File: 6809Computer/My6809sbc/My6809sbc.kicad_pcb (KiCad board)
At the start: 2 copper layers, 155 x 114 mm, 62 parts, among them J1 HEADER 2x5, J10 TP3, J11 A.OUT, J12 HEADER 2x20, J13 5V IN, J2 HEADER 1x6, J3 HEADER 2x5, J4 HEADER 2x5, J5 TP1, J6 TP2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

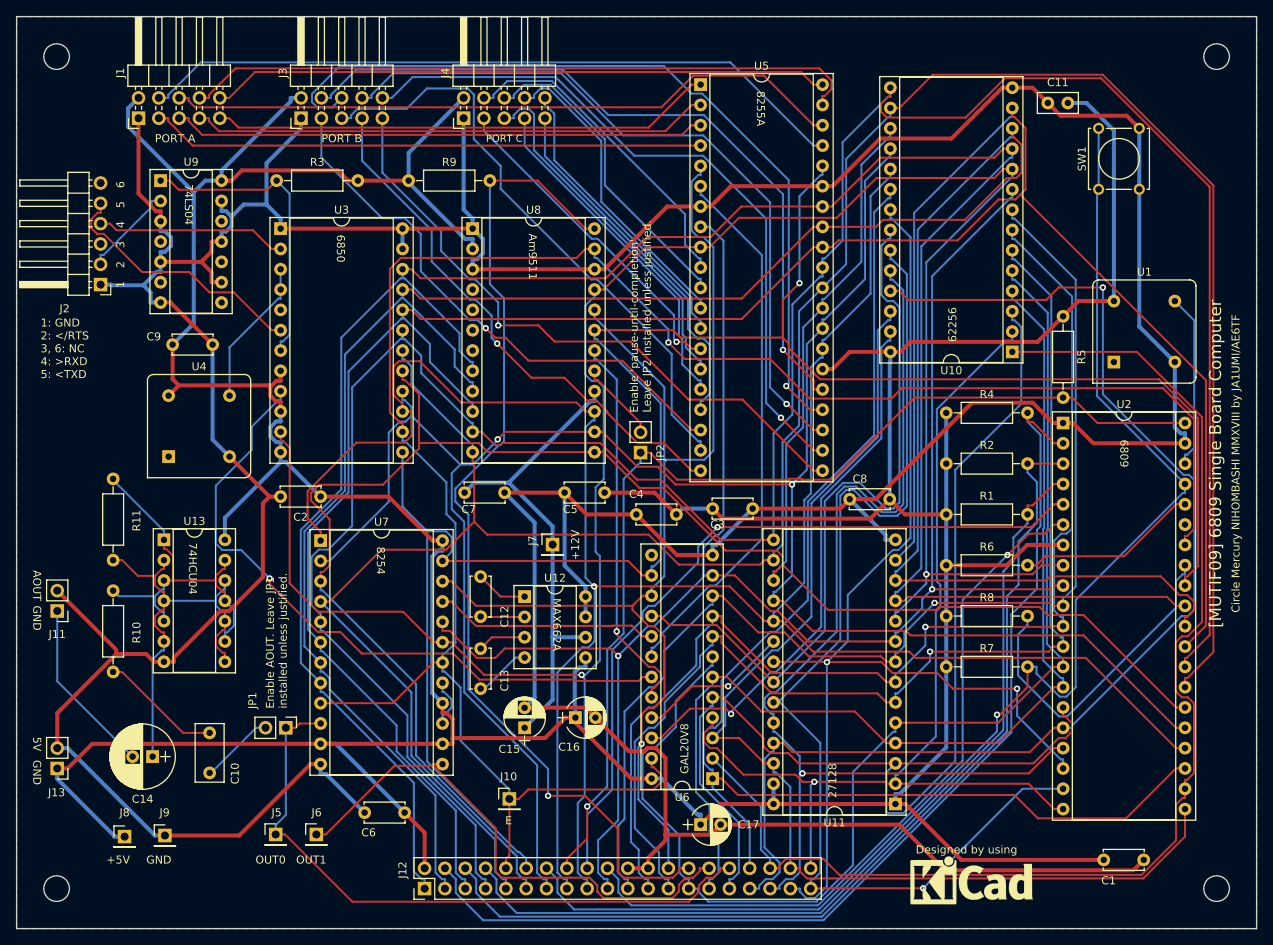
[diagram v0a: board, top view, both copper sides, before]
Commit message: Update design files of 6809 SBC
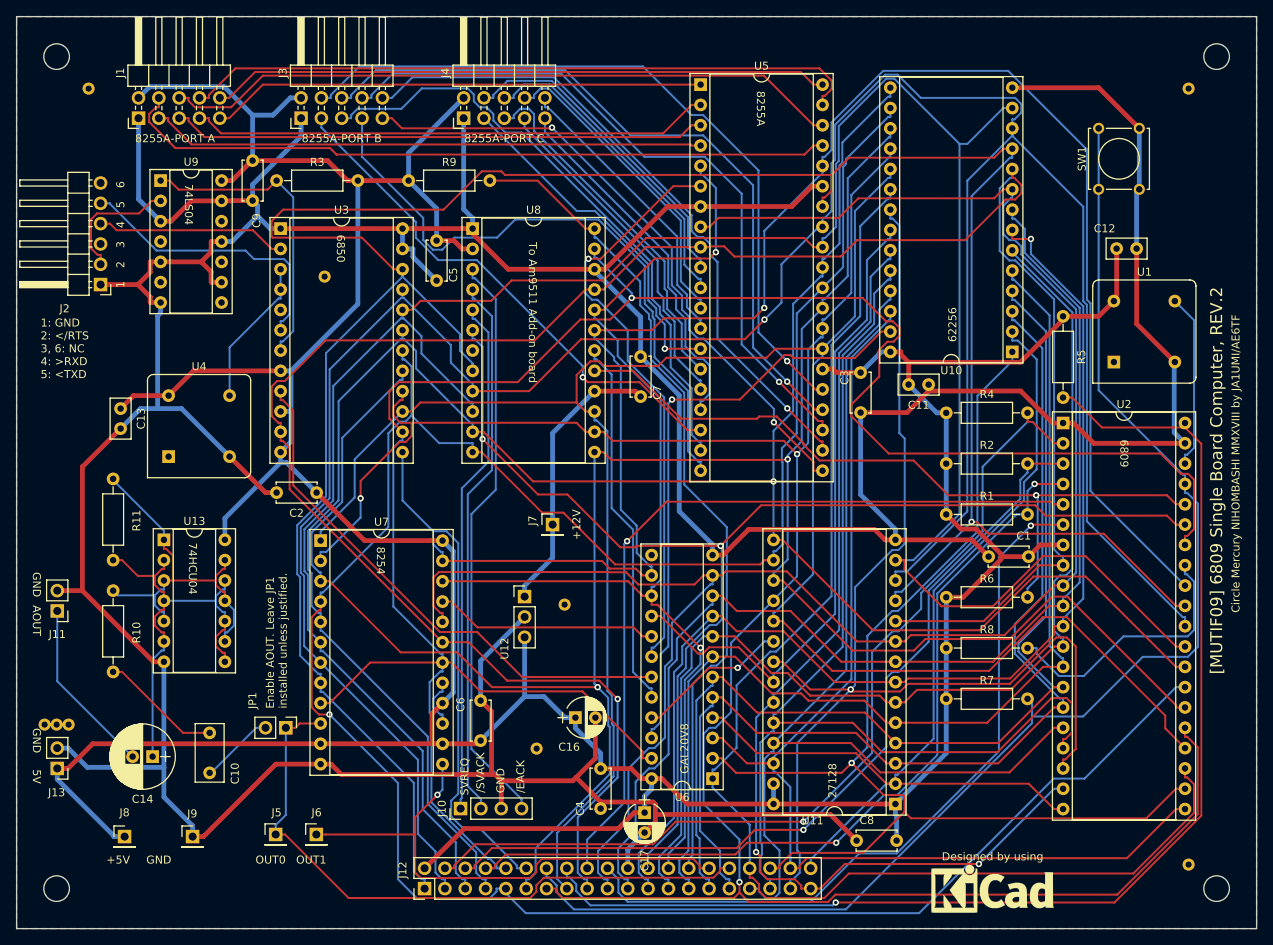
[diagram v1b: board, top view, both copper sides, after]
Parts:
- removed C15: 4.7u, Capacitors_THT:CP_Radial_D5.0mm_P2.50mm
- removed JP2: Enable 'Pause-until-completion', Pin_Headers:Pin_Header_Straight_1x02_Pitch2.54mm
- added REF**: via, mylib:via, F.Cu at (88.5, 62.5)
- added REF**: via, mylib:via, F.Cu at (118.5, 103.5)
- added REF**: via, mylib:via, F.Cu at (115.0, 121.5)
- added REF**: via, mylib:via, F.Cu at (59.0, 39.0)
- added REF**: via, mylib:via, F.Cu at (196.5, 39.0)
- added REF**: via, mylib:via, F.Cu at (196.5, 136.0)
- added REF**: via, mylib:via, F.Cu at (56.5, 118.5)
- added REF**: via, mylib:via, F.Cu at (55.0, 118.5)
- added REF**: via, mylib:via, F.Cu at (53.5, 118.5)
- C12, C13: value 0.22u -> 0.1u; footprint Capacitors_THT:C_Disc_D5.0mm_W2.5mm_P5.00mm -> Capacitors_THT:C_Disc_D5.0mm_W2.5mm_P2.50mm
- C16: value 4.7u -> 47u
- J10: value TP3 -> Conn_01x04; footprint Pin_Headers:Pin_Header_Straight_1x01_Pitch2.54mm -> Pin_Headers:Pin_Header_Straight_1x04_Pitch2.54mm
- J11: value A.OUT -> AUDIO OUT
- J13: value 5V IN -> Conn_01x02
- JP1: value A.OUT enable (normally inst'd) -> PIT Test (normally installed)
- U12: value MAX662A -> U3V12F12; footprint Housings_DIP:DIP-8_W7.62mm_Socket -> Pin_Headers:Pin_Header_Straight_1x03_Pitch2.54mm
- moved C12 91.8 mm to (187.5, 59.0), turned to 0 degrees
- moved C13 54.1 mm to (63.0, 79.0)
- moved C8 42.7 mm to (155.0, 133.0)
- moved C1 39.1 mm to (176.5, 97.5), turned to 180 degrees
- moved C11 38.2 mm to (164.0, 76.0), turned to 180 degrees
- moved C4 37.0 mm to (123.0, 129.0), turned to 90 degrees
- moved C5 31.0 mm to (102.5, 63.0), turned to 90 degrees
- moved C3 25.1 mm to (155.5, 74.5), turned to 270 degrees
- moved C9 25.1 mm to (79.5, 48.0), turned to 270 degrees
- moved C7 25.1 mm to (128.0, 77.5), turned to 90 degrees
- moved C6 13.1 mm to (108.0, 120.5), turned to 90 degrees
- moved C17 7.16 mm to (128.5, 129.5), turned to 270 degrees
- moved J10 6.21 mm to (105.5, 129.0), turned to 90 degrees
- moved R6 4.00 mm to (166.2, 102.6)
- moved R7 4.00 mm to (166.2, 115.3)
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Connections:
- C12 pad 1: Net-(C12-Pad1) -> /+5V
- C12 pad 2: Net-(C12-Pad2) -> /GND
- C13 pad 1: Net-(C13-Pad1) -> /+5V
- C13 pad 2: Net-(C13-Pad2) -> /GND
- J10 pad 1: /E -> Net-(J10-Pad1)
- J12 pad 24: /GND -> /Q
- R6 pad 2: Net-(R6-Pad2) -> /MRDY
- U12 pad 1: Net-(C12-Pad2) -> /+12V
- U12 pad 2: Net-(C12-Pad1) -> /GND
- U12 pad 3: Net-(C13-Pad1) -> /+5V
- U2 pad 35: Net-(U2-Pad35) -> /Q
- U2 pad 36: Net-(R6-Pad2) -> /MRDY
- U8 pad 17: Net-(JP2-Pad2) -> /MRDY
- U8 pad 3: /GND -> Net-(J10-Pad4)
- U8 pad 4: Net-(U8-Pad4) -> Net-(J10-Pad2)
- U8 pad 5: Net-(U8-Pad5) -> Net-(J10-Pad1)
- U8 pad 6: Net-(U8-Pad6) -> /Q
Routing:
- net /Q: track 0.00 -> 155.5 mm, vias 0 -> 2
- net /MRDY: track 0.00 -> 94.4 mm, vias 0 -> 1
- net /+5V: track 594.1 -> 513.0 mm
- net Net-(J10-Pad4): track 0.00 -> 72.6 mm
- net Net-(J10-Pad2): track 0.00 -> 67.9 mm
- net Net-(J10-Pad1): track 0.00 -> 64.8 mm
- net /D3: track 321.1 -> 266.8 mm, vias 0 -> 1
- net /D1: track 299.1 -> 337.2 mm, vias 0 -> 1
- net /D0: track 288.3 -> 320.9 mm, vias 0 -> 1
- net /A8: track 156.1 -> 127.5 mm, vias 1 -> 0
- net /A7: track 159.8 -> 132.0 mm
- net /GND: track 655.7 -> 628.9 mm
- net /+12V: track 60.7 -> 35.3 mm
- net //HALT: track 130.9 -> 153.8 mm
- net Net-(R6-Pad2): track 22.8 -> 0.00 mm
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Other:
- net class Power: trace_width 0.5 -> 0.6
- board text added: "/EACK"
- board text added: "/SVACK"
- board text added: "8255A-PORT A"
- board text added: "8255A-PORT B"
- board text added: "8255A-PORT C"
- board text added: "SVREQ"
- board text added: "To Am9511 Add-on board"
- board text added: "[MUTIF09] 6809 Single Board Computer, REV.2"
- board text removed: "Am9511"
- board text removed: "E"
- board text removed: "Enable 'pause-until-completion' Leave JP2 installed unless justified."
- board text removed: "MAX662A"
- board text removed: "PORT A"
- board text removed: "PORT B"
- board text removed: "PORT C"
- board text removed: "[MUTIF09] 6809 Single Board Computer"

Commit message: Update design materials of 6809sbc and old files are moved to the archive directory (REV2). Now My6809sbc directory contains REV3 design materials.
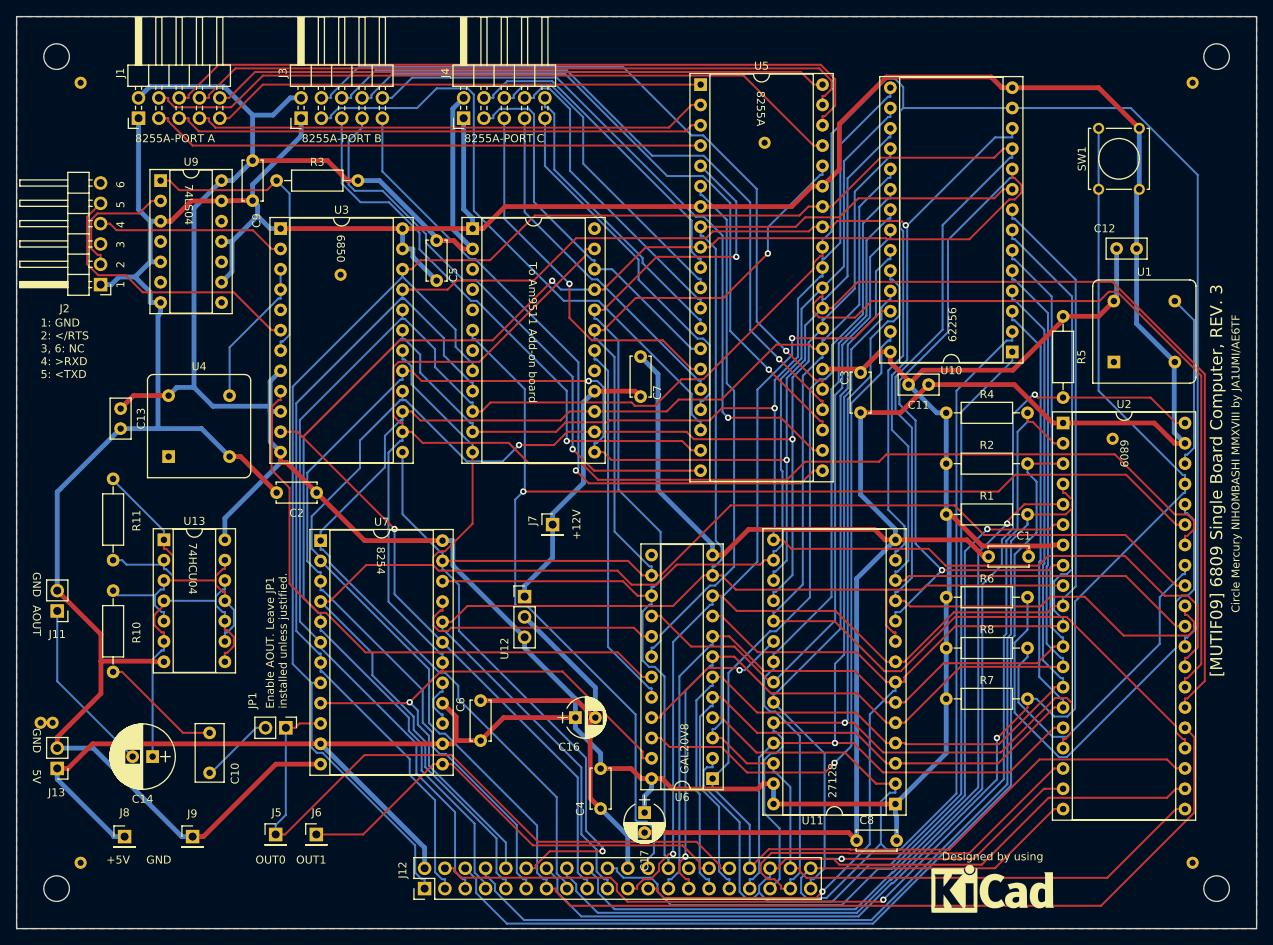
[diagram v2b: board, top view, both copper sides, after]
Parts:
- removed J10: Conn_01x04, Pin_Headers:Pin_Header_Straight_1x04_Pitch2.54mm
- removed R9: 2.2k, Resistors_THT:R_Axial_DIN0207_L6.3mm_D2.5mm_P10.16mm_Horizontal
- removed REF** (x9): via, mylib:via
- added ?: via, sbclib:via, F.Cu at (143.5, 44.5)
- added ?: via, sbclib:via, F.Cu at (197.0, 37.0)
- added ?: via, sbclib:via, F.Cu at (197.0, 134.5)
- added ?: via, sbclib:via, F.Cu at (58.0, 37.0)
- added ?: via, sbclib:via, F.Cu at (90.5, 61.0)
- added ?: via, sbclib:via, F.Cu at (54.5, 117.0)
- added ?: via, sbclib:via, F.Cu at (58.0, 134.5)
- added ?: via, sbclib:via, F.Cu at (53.0, 117.0)
- added ?: via, sbclib:via, F.Cu at (187.0, 81.5)
- R1, R2, R4, R5, R6, R7, R8: value 2.2k -> 10k
- U8: value Am9511 -> HEADER 2x12
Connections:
- J12 pad 28: //END -> Net-(J12-Pad28)
- U8 pad 17: /MRDY -> Net-(U8-Pad17)
- U8 pad 22: /GND -> /PC0
- U8 pad 24: //END -> Net-(U8-Pad24)
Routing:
- net //END: track 104.9 -> 0.00 mm
- net Net-(U8-Pad3): track 72.6 -> 0.00 mm
- net Net-(U8-Pad4): track 67.9 -> 0.00 mm
- net Net-(U8-Pad5): track 64.8 -> 0.00 mm
- net /D1: track 337.2 -> 275.7 mm
- net /D2: track 307.1 -> 344.5 mm
- net /MRDY: track 94.4 -> 63.2 mm, vias 1 -> 0
- net /A12: track 129.9 -> 159.9 mm
- net /R_/W: track 274.7 -> 246.0 mm, vias 1 -> 2
- net /A14: track 145.9 -> 172.3 mm, vias 1 -> 0
- net /D0: track 320.9 -> 298.4 mm, vias 1 -> 0
- net //HALT: track 153.8 -> 134.2 mm
- net /GND: track 628.9 -> 648.3 mm
- net //IRQ: track 106.7 -> 125.7 mm, vias 1 -> 0
- net /A1: track 235.2 -> 216.7 mm
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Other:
- board text added: "[MUTIF09] 6809 Single Board Computer, REV. 3"
- board text removed: "/EACK"
- board text removed: "/SVACK"
- board text removed: "SVREQ"
- board text removed: "[MUTIF09] 6809 Single Board Computer, REV.2"
